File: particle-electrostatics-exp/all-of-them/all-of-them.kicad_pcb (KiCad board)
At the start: 2 copper layers, 164.5 x 113 mm, 92 parts, among them J1 Screw_Terminal_01x04, J2 Screw_Terminal_01x04, J5 Screw_Terminal_01x04, J6 Screw_Terminal_01x04, SW2 SW_SPDT_321, U1 LMC6082, U4 MAX1032BEUG_

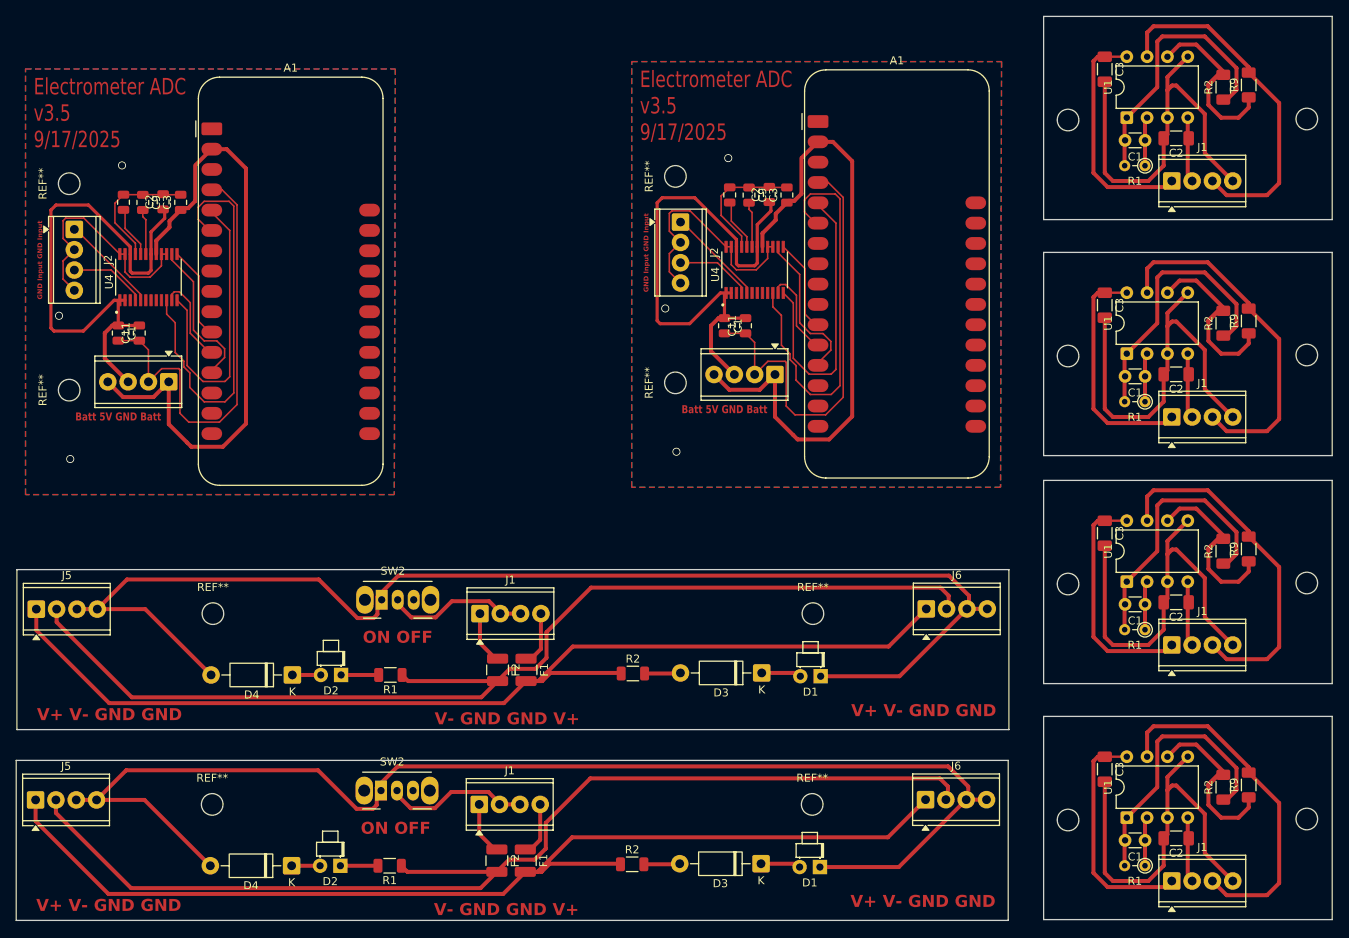
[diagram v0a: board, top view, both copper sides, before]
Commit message: updated pcb layout slightly
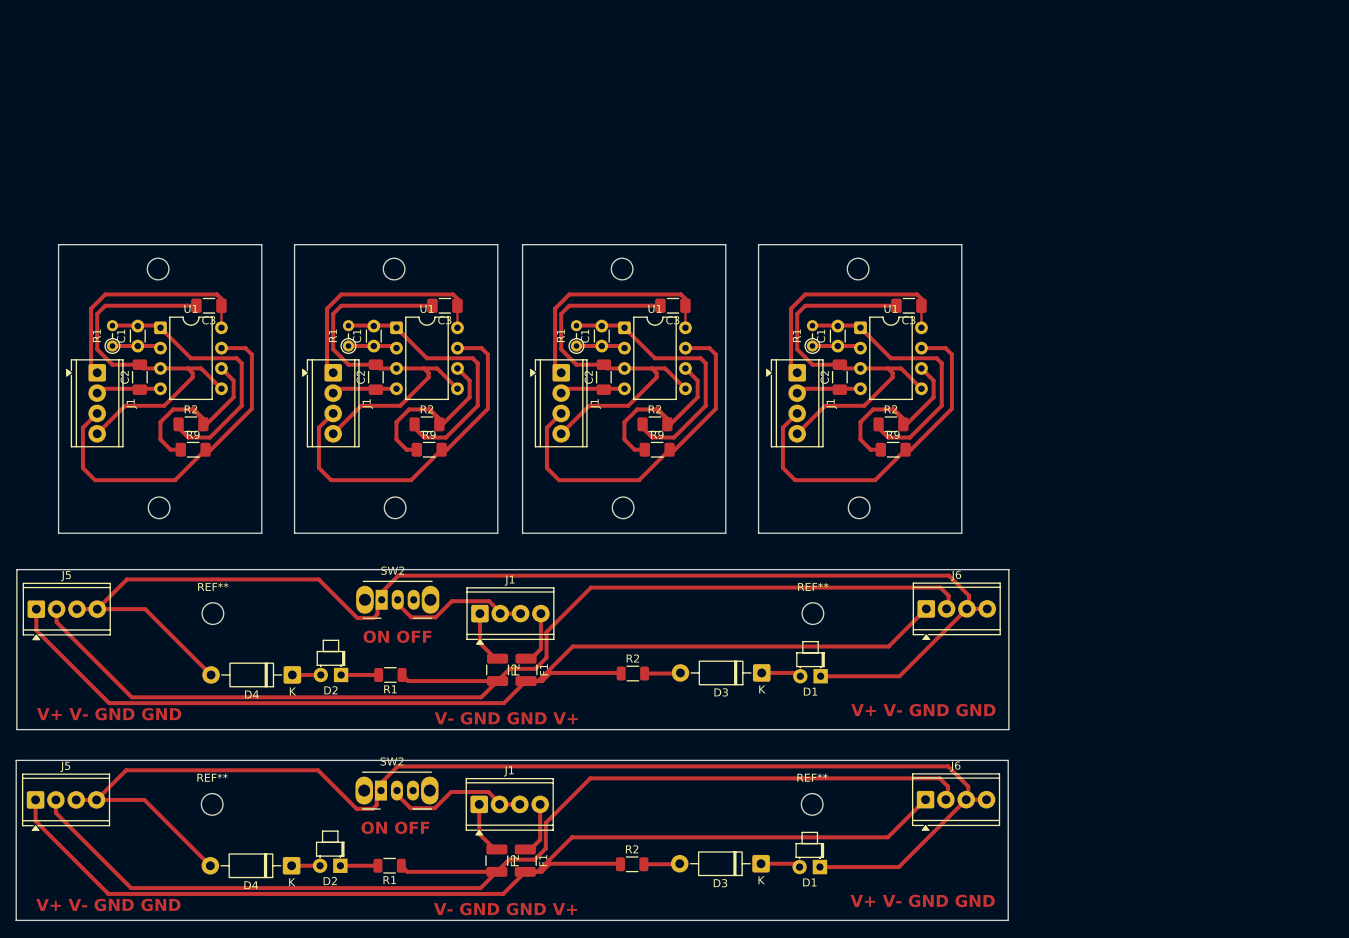
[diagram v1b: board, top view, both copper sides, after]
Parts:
- removed A1 (x2): Adafruit_Feather_Generic, Adafruit:Adafruit_Feather_NTHP
- removed the C1 at (141.5, 91.7)
- removed the C1 at (65.8, 92.6)
- removed C11 (x2), C9 (x2): 100n, Capacitor_SMD:C_0805_2012Metric
- removed the C2 at (71.4, 76.2)
- removed the C2 at (147.1, 75.3)
- removed the C3 at (73.6, 76.2)
- removed the C3 at (149.3, 75.3)
- removed C8 (x2): 1u, Capacitor_SMD:C_0805_2012Metric
- removed the J1 at (72.1, 98.7)
- removed the J1 at (147.8, 97.8)
- removed J2 (x2): Screw_Terminal_01x04, TerminalBlock_Phoenix:TerminalBlock_Phoenix_MPT-0,5-4-2.54_1x04_P2.54mm_Horizontal
- removed the REF** at (135.4, 98.8)
- removed the REF** at (59.6, 73.9)
- removed the REF** at (135.4, 73.0)
- removed the REF** at (59.6, 99.7)
- removed U4 (x2): MAX1032BEUG_, Max1032:SOP65P640X110-24N
- moved REF** 148.6 mm to (70.9, 114.4), turned to 0 degrees
- moved J1 148.6 mm to (63.1, 97.6), turned to -90 degrees
- moved R1 144.5 mm to (65.0, 94.2), turned to 90 degrees
- moved C2 141.8 mm to (68.5, 98.1), turned to 90 degrees
- moved C1 140.2 mm to (68.2, 94.2), turned to 90 degrees
- moved R9 138.4 mm to (75.1, 107.2), turned to 0 degrees
- moved R2 136.8 mm to (74.8, 104.0), turned to 0 degrees
- moved U1 135.4 mm to (71.0, 91.9), turned to 0 degrees
- moved REF** 133.0 mm to (70.7, 84.6), turned to 0 degrees
- moved C3 126.1 mm to (77.1, 89.2), turned to 180 degrees
- moved REF** 114.3 mm to (100.4, 114.4), turned to 0 degrees
- moved J1 110.2 mm to (92.6, 97.6), turned to -90 degrees
- moved R1 105.7 mm to (94.5, 94.2), turned to 90 degrees
- moved C2 103.9 mm to (98.0, 98.1), turned to 90 degrees
- moved R9 103.2 mm to (104.6, 107.2), turned to 0 degrees
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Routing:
- net GND: track 734.9 -> 530.4 mm, vias 6 -> 0
- net +BATT: track 426.9 -> 266.7 mm
- net +5V: track 135.3 -> 0.00 mm
- net /~{CS}: track 101.6 -> 0.00 mm
- net /SSTRB: track 73.9 -> 0.00 mm
- net /MISO: track 38.5 -> 0.00 mm
- net Net-(J2-Pin_1): track 24.8 -> 0.00 mm
- net /SCK: track 22.8 -> 0.00 mm
- net /MOSI: track 21.9 -> 0.00 mm
- net Net-(J2-Pin_3): track 19.3 -> 0.00 mm
- net Net-(U4-REF): track 12.8 -> 0.00 mm
- net Net-(U4-REFCAP): track 11.9 -> 0.00 mm
- removed copper zone on B.Cu, net GND
- removed copper zone on F.Cu, net GND
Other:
- board size 164.5 x 113 mm -> 124.1 x 84.5 mm
- board text removed: "Batt 5V GND Batt"
- board text removed: "Electrometer ADC v3.5 9/17/2025"
- board text removed: "GND Input GND Input"
